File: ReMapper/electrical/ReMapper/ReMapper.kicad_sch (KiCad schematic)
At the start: 51 parts, among them J2 USB_IN, J5 USB_OUT, U1 ESP32-S3-WROOM-1-N8R8, U2 RP2040, U3 W25Q128JVE, U4 RT6150B-33GQW, U5 W25Q128JVE, Y1 12MHZ

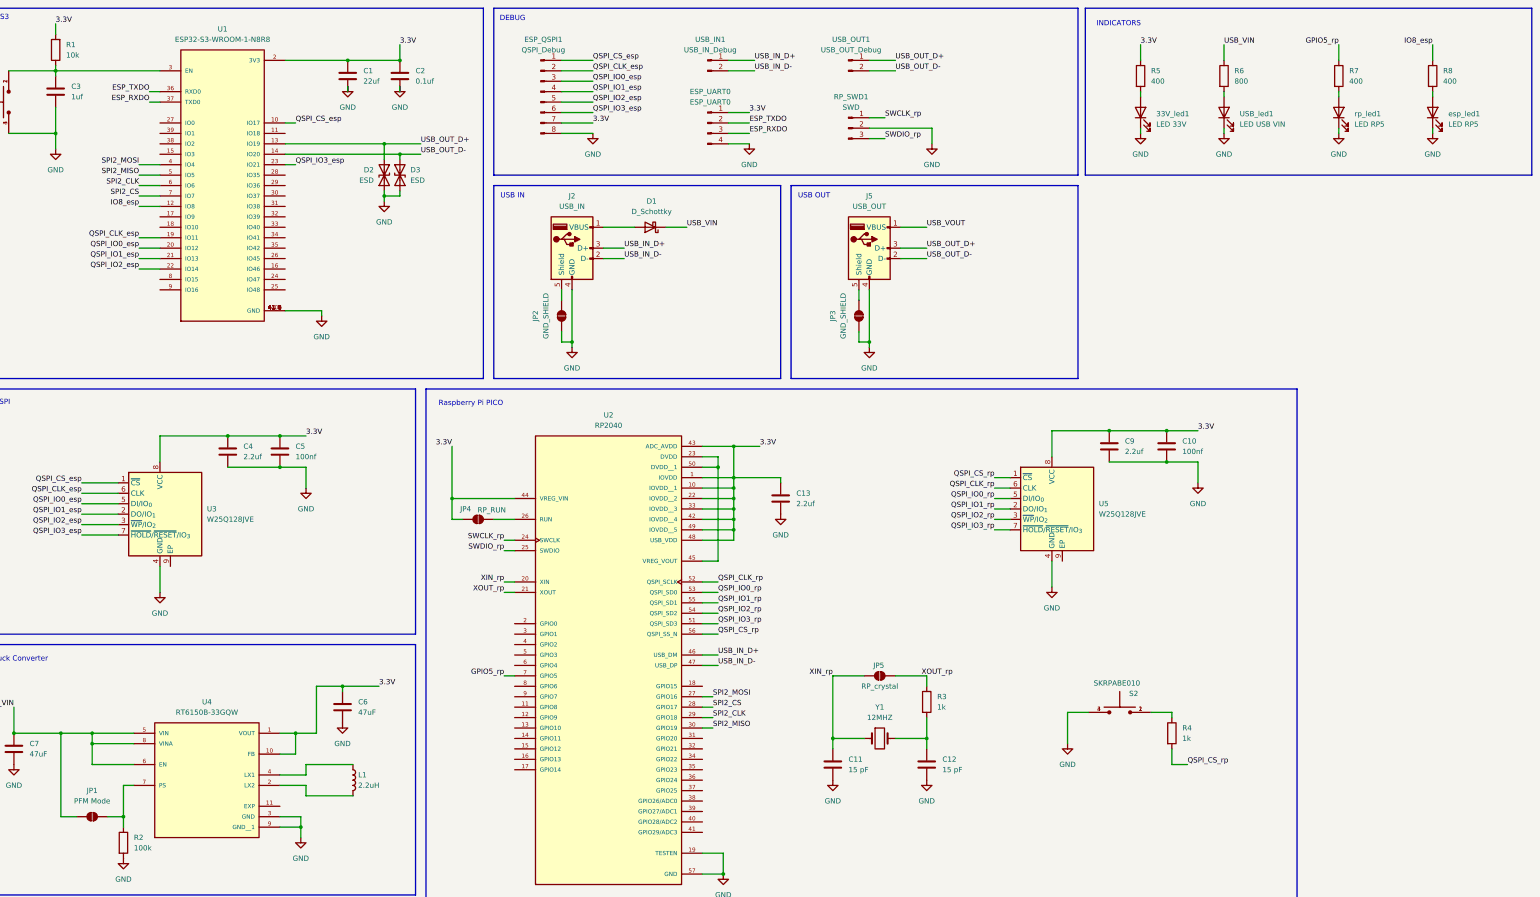
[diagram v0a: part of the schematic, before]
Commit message: low lcsc inventory on some parts, switch to standard lib instead of extended for them. for the Crystal and Boost Convertor
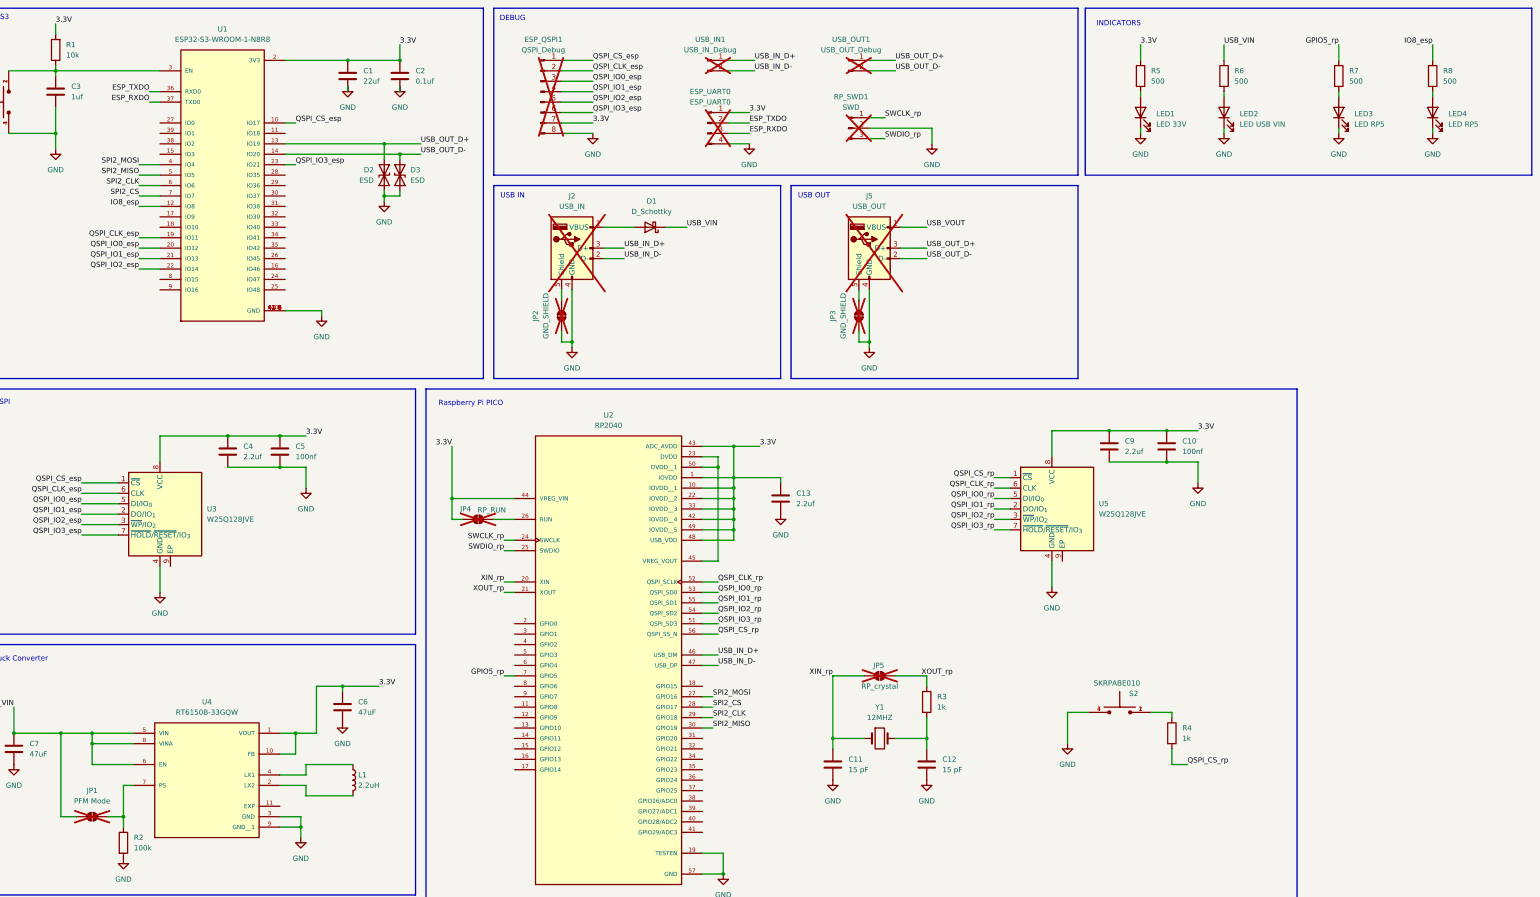
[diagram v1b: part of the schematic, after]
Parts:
- C1: LCSC Part (none) -> C48579267
- C10, C3, C5: LCSC Part (none) -> C5189821
- C11, C12: LCSC Part (none) -> C107037
- C13, C4, C9: LCSC Part (none) -> C5189830
- C2: LCSC Part (none) -> C14663
- C6, C7, C8: LCSC Part (none) -> C140782
- D1: LCSC Part (none) -> C82544
- D2, D3, D4, D5: LCSC Part (none) -> SOD523
- ESP_QSPI1, ESP_UART0, J2, J5, RP_SWD1, USB_IN1, USB_OUT1: now not fitted; now left out of the parts list
- JP1, JP2, JP3, JP4, JP5: now not fitted
- L1: LCSC Part (none) -> C560036
- LED1: renamed from 33V_led1; LCSC Part (none) -> C965807
- LED2: renamed from USB_led1; LCSC Part (none) -> C965807
- LED3: renamed from rp_led1; LCSC Part (none) -> C965807
- LED4: renamed from esp_led1; LCSC Part (none) -> C965807
- R1: LCSC Part (none) -> C98220
- R2: LCSC Part (none) -> C14675
- R3, R4: LCSC Part (none) -> C22548
- R5, R7, R8: value 400 -> 500; LCSC Part (none) -> C860931
- R6: value 800 -> 500; LCSC Part (none) -> C860931
- S1, S2: LCSC Part (none) -> C115360
- U1: LCSC Part (none) -> C2913201
- U2: LCSC Part (none) -> C2040
- U3, U5: LCSC Part (none) -> C401662
- U4: LCSC Part (none) -> C3187669
- Y1: LCSC Part (none) -> C6204593

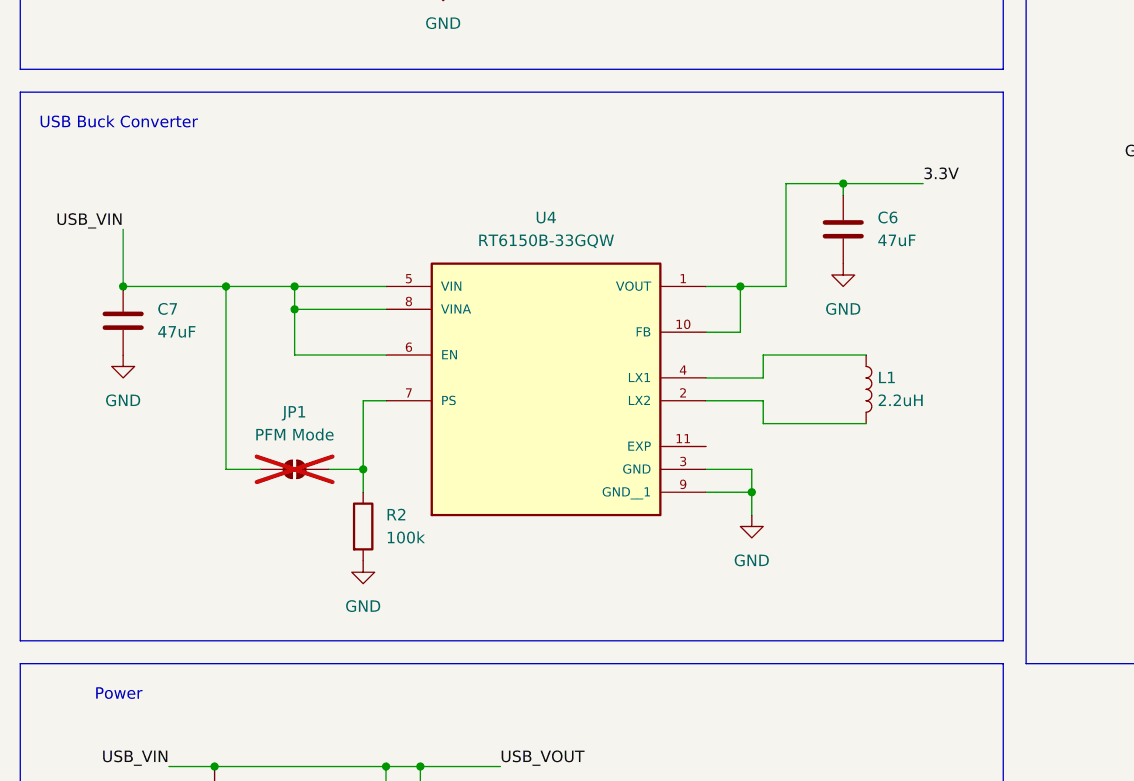
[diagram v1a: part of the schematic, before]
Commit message: picked basic parts from lcsc, pre fab
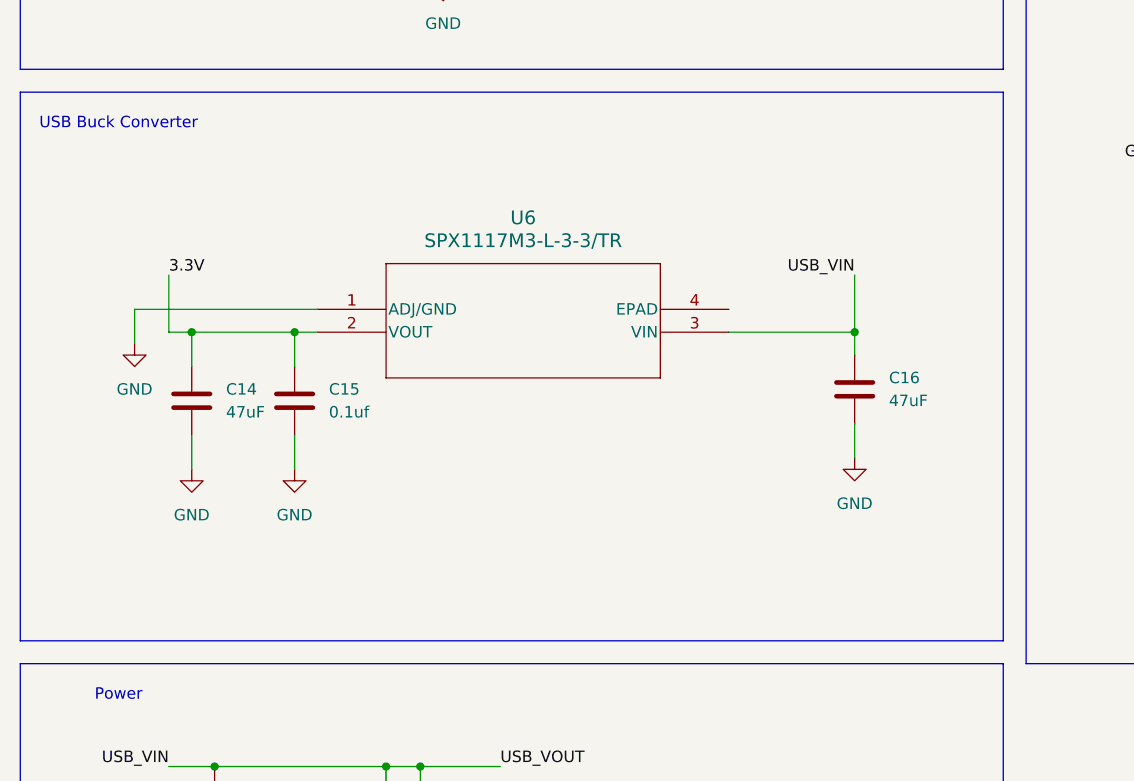
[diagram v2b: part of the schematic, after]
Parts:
- removed C6, C7: 47uF, Capacitor_SMD:C_0603_1608Metric, symbol Device:C
- removed JP1: PFM Mode, Jumper:SolderJumper-2_P1.3mm_Open_Pad1.0x1.5mm, symbol Jumper:SolderJumper_2_Open
- removed L1: 2.2uH, Inductor_SMD:L_0603_1608Metric, symbol Device:L
- removed R2: 100k, Resistor_SMD:R_0603_1608Metric, symbol Device:R
- removed U4: RT6150B-33GQW, footprints:RT6150B-33GQW, symbol RT6150B-33GQW:RT6150B-33GQW
- added C14, C16: 47uF, Capacitor_SMD:C_0603_1608Metric, symbol Device:C
- added C15: 0.1uf, Capacitor_SMD:C_0603_1608Metric, symbol Device:C
- added U6: SPX1117M3-L-3-3/TR, Package_TO_SOT_SMD:SOT-223, symbol SPX1117M3_L:SPX1117M3-L-3-3_TR
- Y1: footprint Crystal:Crystal_HC49-4H_Vertical -> Crystal:Crystal_SMD_3225-4Pin_3.2x2.5mm; LCSC Part C6204593 -> C9002
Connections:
- net 3.3V: now also C14.1, C15.1, U6.2 (VOUT)
- net GND: now also C14.2, C15.2, C16.2, U6.1 (ADJ/GND)
- net USB_VIN: now also C16.1, U6.3 (VIN)

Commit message: fixed up V1, added some debug. Now working on V2
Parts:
- removed Y1: 12MHZ, Crystal:Crystal_SMD_3225-4Pin_3.2x2.5mm, symbol Device:Crystal
- added JP1: VIN_Schottky, Jumper:SolderJumper-2_P1.3mm_Open_Pad1.0x1.5mm, symbol Jumper:SolderJumper_2_Open
- added S3: SKRPABE010, footprints:push_button_SKRPABE010, symbol push_button_SKRPABE010:SKRPABE010
- added Y2: 12MHZ, Crystal:Crystal_SMD_3225-4Pin_3.2x2.5mm, symbol Device:Crystal_GND24
- ESP_QSPI1: footprint Connector_PinHeader_1.00mm:PinHeader_1x08_P1.00mm_Vertical -> Connector_PinHeader_2.54mm:PinHeader_1x08_P2.54mm_Vertical
- ESP_UART0: footprint Connector_PinHeader_1.00mm:PinHeader_1x04_P1.00mm_Vertical -> Connector_PinHeader_2.54mm:PinHeader_1x04_P2.54mm_Vertical
- RP_SWD1: footprint Connector_PinHeader_1.00mm:PinHeader_1x03_P1.00mm_Vertical -> Connector_PinHeader_2.54mm:PinHeader_1x03_P2.54mm_Vertical
- USB_IN1, USB_OUT1: footprint Connector_PinHeader_1.00mm:PinHeader_1x02_P1.00mm_Vertical -> Connector_PinHeader_2.54mm:PinHeader_1x02_P2.54mm_Vertical
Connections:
- net GND: now also S3.3, S3.4, Y2.2, Y2.4
- net USB_IN_D+: now also U2.47 (USB_DP); no longer U2.46 (USB_DM)
- net USB_IN_D-: now also U2.46 (USB_DM); no longer U2.47 (USB_DP)
- net USB_VIN: now also JP1.2 (B)
- net XIN_rp: now also Y2.1
- net at D1.2 (A), J2.1 (VBUS): now also JP1.1 (A)
- net at C12.1, R3.2: now also Y2.3
- net ESP_IO0: now reaches U1.27 (IO0)
- net ESP_IO0: now also S3.1, S3.2
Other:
- moved on the sheet: C11, C12, D1, J2, JP2, JP5, R3

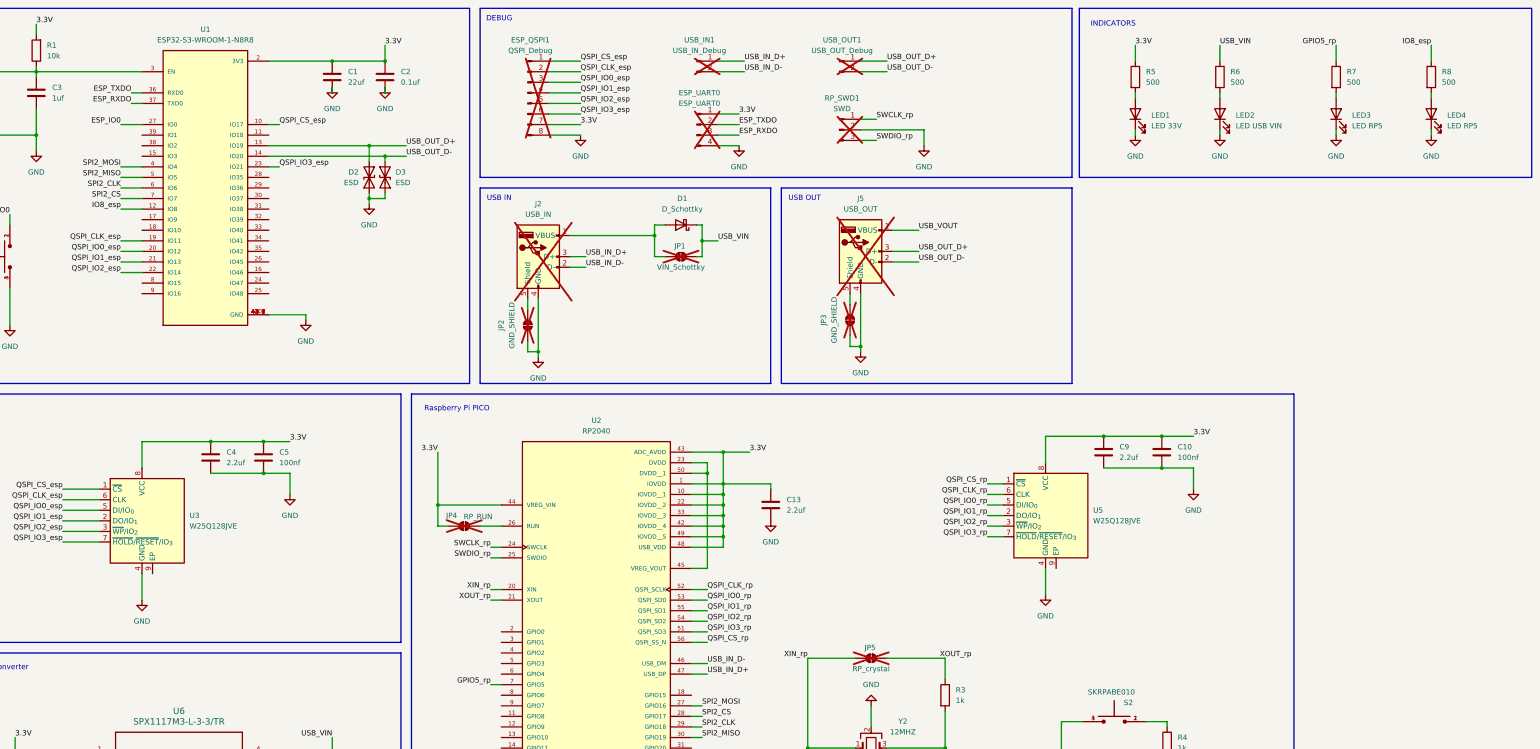
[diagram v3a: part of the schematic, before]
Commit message: Remapper started V2 Layout
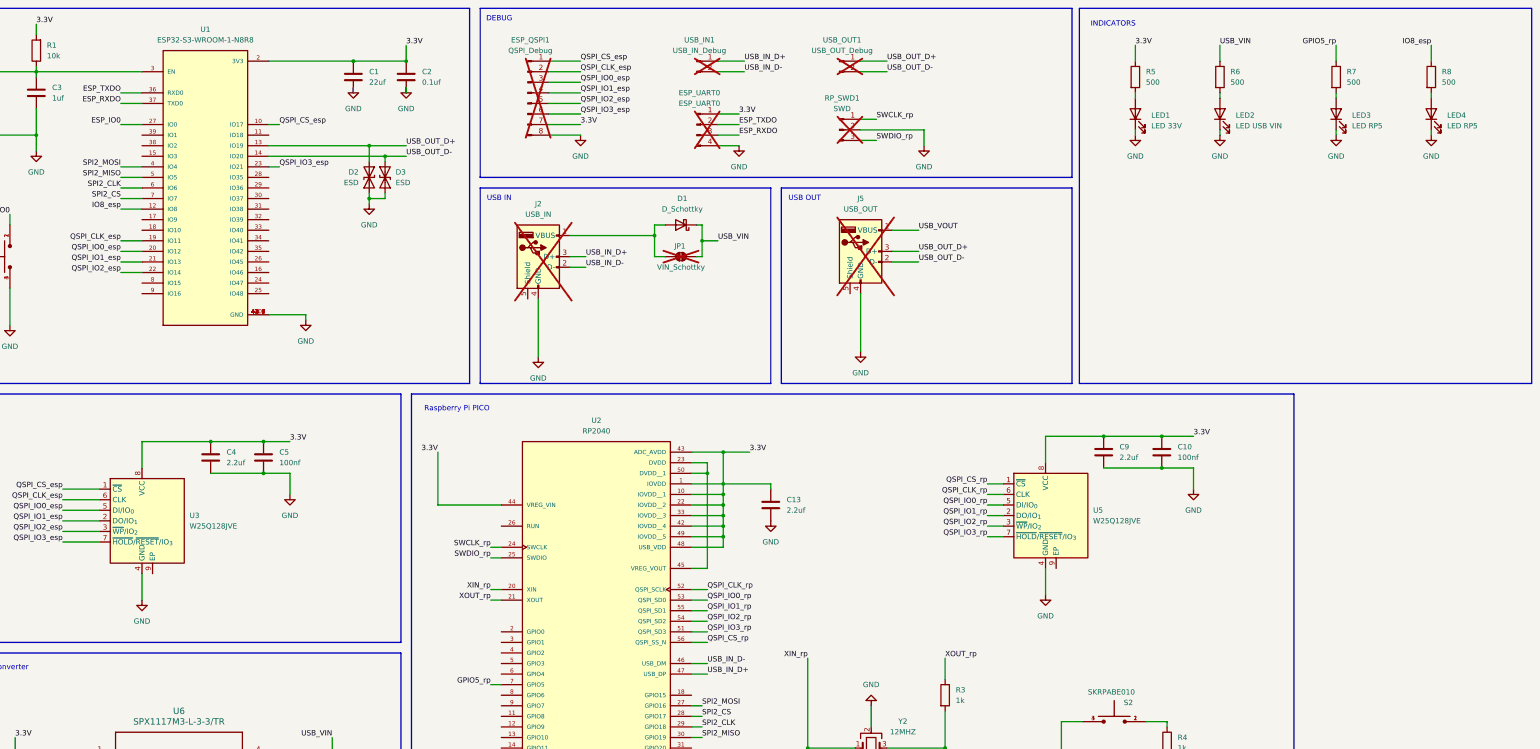
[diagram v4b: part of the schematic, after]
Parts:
- removed JP2, JP3: GND_SHIELD, Jumper:SolderJumper-2_P1.3mm_Open_Pad1.0x1.5mm, symbol Jumper:SolderJumper_2_Open
- removed JP4: RP_RUN, Jumper:SolderJumper-2_P1.3mm_Open_Pad1.0x1.5mm, symbol Jumper:SolderJumper_2_Open
- removed JP5: RP_crystal, Jumper:SolderJumper-2_P1.3mm_Open_Pad1.0x1.5mm, symbol Jumper:SolderJumper_2_Open
- J5: footprint Connector_PinHeader_1.00mm:PinHeader_1x04_P1.00mm_Vertical -> Connector_PinHeader_2.54mm:PinHeader_1x05_P2.54mm_Vertical
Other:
- moved on the sheet: C1, C2

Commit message: V2 passing DRC
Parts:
- removed USB_OUT1: USB_OUT_Debug, Connector_PinHeader_2.54mm:PinHeader_1x02_P2.54mm_Vertical, symbol Connector:Conn_01x02_Pin
- U1: footprint footprints:XCVR_ESP32S3WROOM1N8R8 -> RF_Module:ESP32-S3-WROOM-1
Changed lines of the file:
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@@
 	(wire
 		(pts
-			(xy 245.11 29.21) (xy 251.46 29.21)
-		)
-		(stroke
-			(width 0)
-			(type default)
-		)
-	)
-	(wire
-		(pts
 			(xy 313.69 187.96) (xy 318.77 187.96)
 		)
@@
 	(wire
 		(pts
-			(xy 245.11 31.75) (xy 251.46 31.75)
-		)
-		(stroke
-			(width 0)
-			(type default)
-		)
-	)
-	(wire
-		(pts
 			(xy 207.01 184.15) (xy 204.47 184.15)
 		)
@@
 		)
 	)
-	(label "USB_OUT_D+"
-		(at 251.46 29.21 0)
-		(effects
-			(font
-				(size 1.27 1.27)
-			)
-			(justify left bottom)
-		)
-	)
-	(label "USB_OUT_D-"
-		(at 251.46 31.75 0)
-		(effects
-			(font
-				(size 1.27 1.27)
-			)
-			(justify left bottom)
-		)
-	)
 	(label "USB_VIN"
 		(at 41.91 246.38 180)
@@
 	)
 	(symbol
-		(lib_id "Connector:Conn_01x02_Pin")
-		(at 240.03 29.21 0)
-		(unit 1)
-		(exclude_from_sim no)
-		(in_bom no)
-		(on_board yes)
-		(dnp yes)
-		(fields_autoplaced yes)
-		(property "Reference" "USB_OUT1"
-			(at 240.665 24.13 0)
-			(effects
-				(font
-					(size 1.27 1.27)
-				)
-			)
-		)
-		(property "Value" "USB_OUT_Debug"
-			(at 240.665 26.67 0)
-			(effects
-				(font
-					(size 1.27 1.27)
-				)
-			)
-		)
-		(property "Footprint" "Connector_PinHeader_2.54mm:PinHeader_1x02_P2.54mm_Vertical"
-			(at 240.03 29.21 0)
-			(effects
-				(font
-					(size 1.27 1.27)
-				)
-				(hide yes)
-			)
-		)
-		(property "Datasheet" "~"
-			(at 240.03 29.21 0)
-			(effects
-				(font
-					(size 1.27 1.27)
-				)
-				(hide yes)
-			)
-		)
-		(property "Description" "Generic connector, single row, 01x02, script generated"
-			(at 240.03 29.21 0)
-			(effects
-				(font
-					(size 1.27 1.27)
-				)
-				(hide yes)
-			)
-		)
-		(property "SNAPEDA_PACKAGE_ID" ""
-			(at 240.03 29.21 0)
-			(effects
-				(font
-					(size 1.27 1.27)
-				)
-				(hide yes)
-			)
-		)
-		(pin "1"
-		)
-		(pin "2"
-		)
-		(instances
-			(project "ReMapper"
-				(path "/facd47ac-9f29-4b3c-ae50-ce7a688e305d"
-					(reference "USB_OUT1")
-					(unit 1)
-				)
-			)
-		)
-	)
-	(symbol
 		(lib_id "power:GND")
 		(at 215.9 49.53 0)
@@
 			)
 		)
-		(property "Footprint" "footprints:XCVR_ESP32S3WROOM1N8R8"
+		(property "Footprint" "RF_Module:ESP32-S3-WROOM-1"
 			(at 87.63 59.69 0)
 			(effects
